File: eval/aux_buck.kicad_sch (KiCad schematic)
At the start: 15 parts, among them U1 AP63205WU-7, U10 TPS7A2033PDBVR, U12 TPS7A2033PDBVR

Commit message: [layout] layout completed, ready for trace
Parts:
- R17: footprint (none) -> Resistor_SMD:R_0603_1608Metric
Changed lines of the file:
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@@
 			)
 		)
-		(property "Footprint" ""
+		(property "Footprint" "Resistor_SMD:R_0603_1608Metric"
 			(at 97.79 118.11 0)
 			(hide yes)

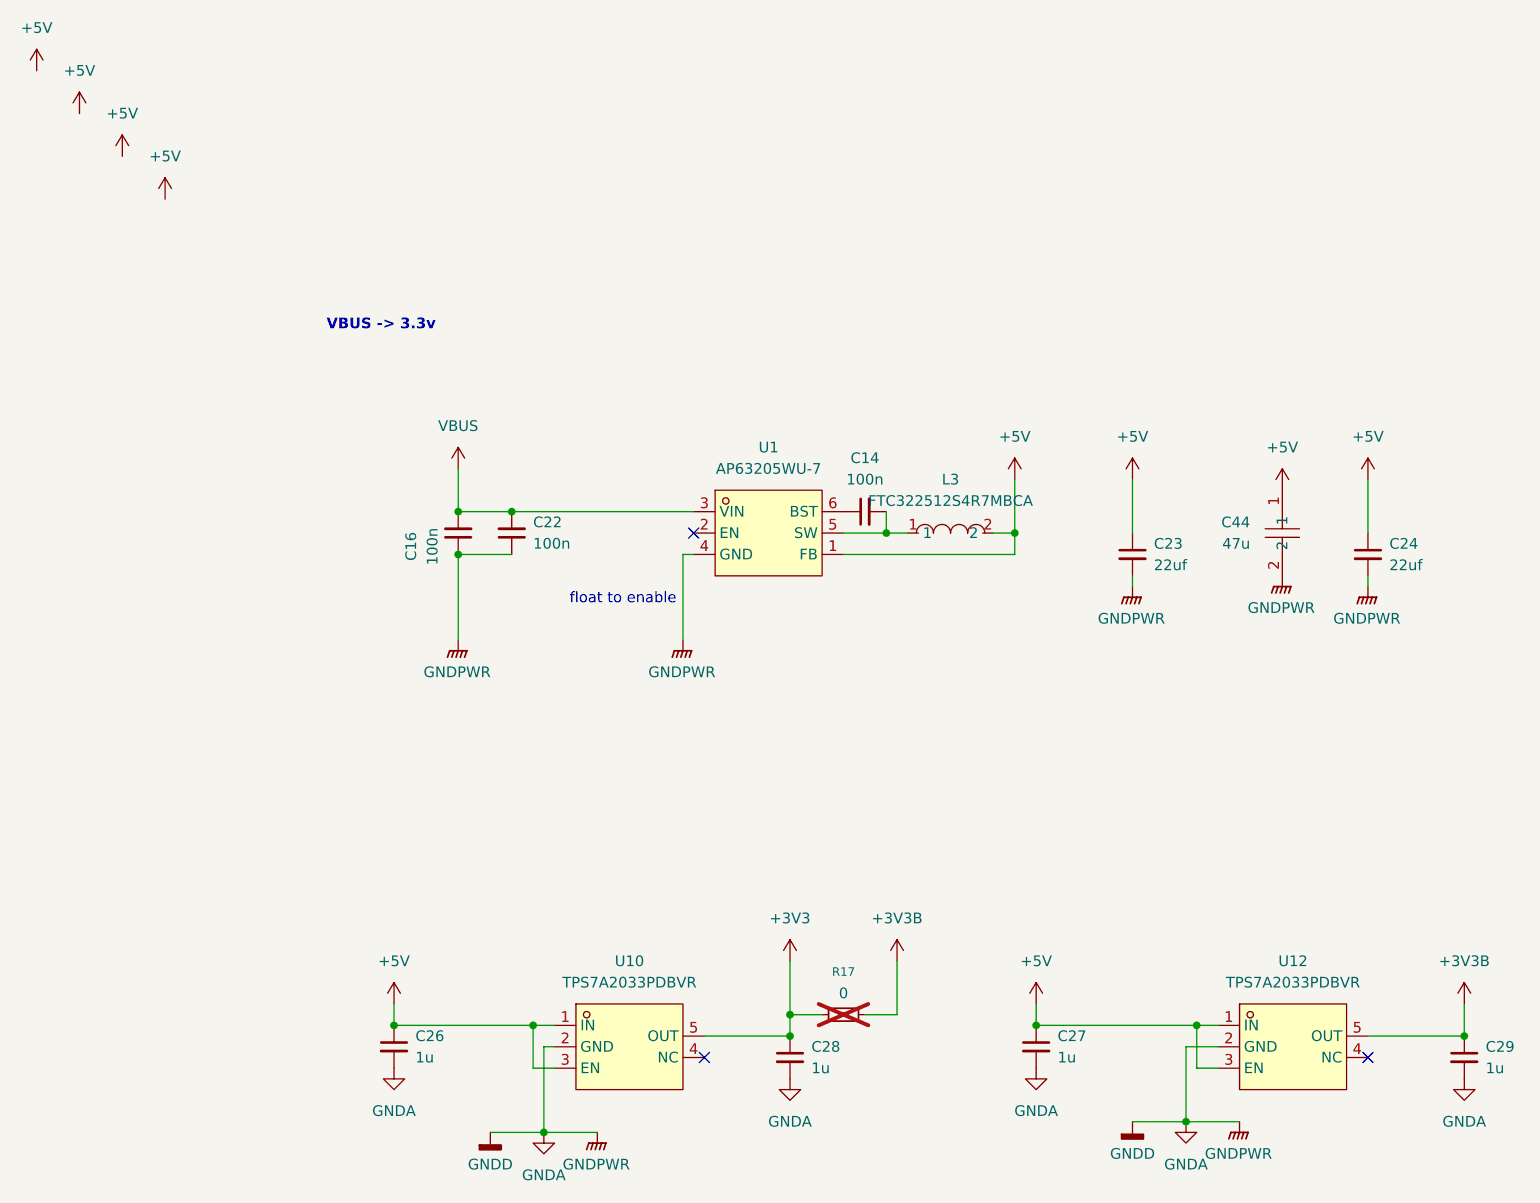
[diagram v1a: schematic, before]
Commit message: [trace] add high power trace
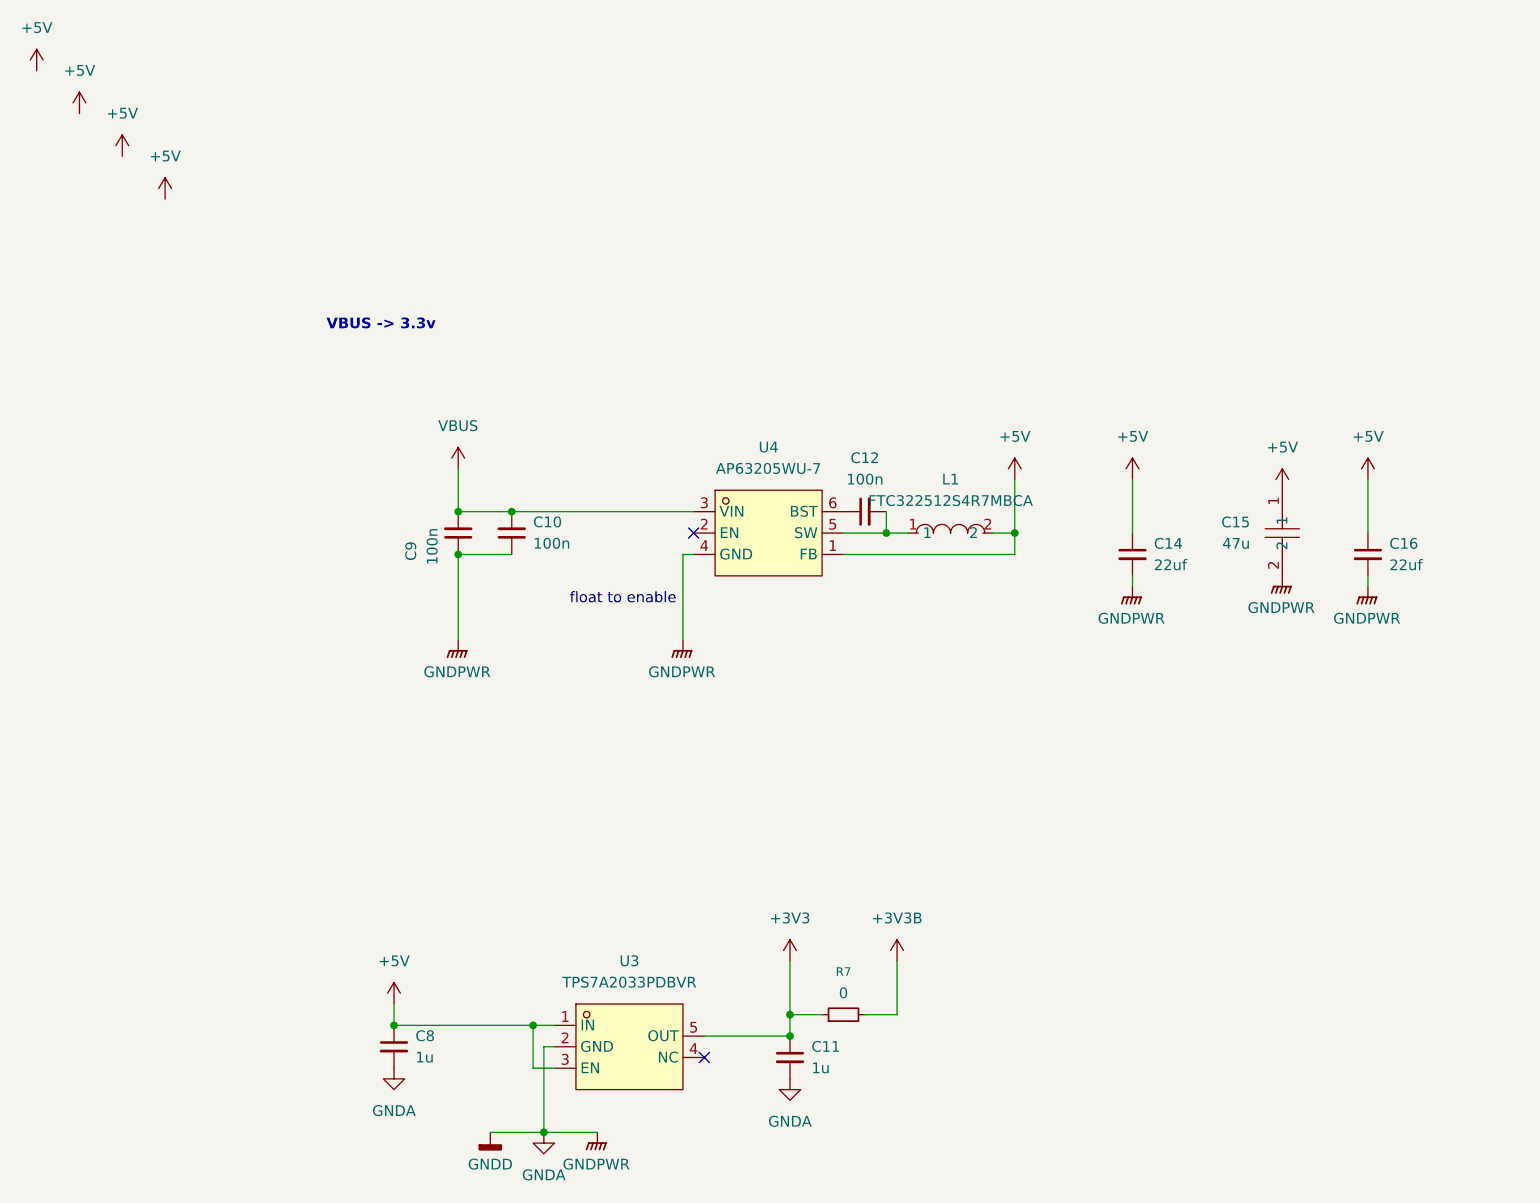
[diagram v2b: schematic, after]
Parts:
- removed C27, C29: 1u, Capacitor_SMD:C_0603_1608Metric, symbol Device:C_Small
- removed U12: TPS7A2033PDBVR, EasyEDA:SOT-23-5_L2.9-W1.6-P0.95-LS2.8-BR, symbol EasyEDA:TPS7A2033PDBVR
- R7: renamed from R17; now fitted
- renumbered C22 to C10, C28 to C11, C14 to C12, C23 to C14, C44 to C15, C24 to C16, C26 to C8, C16 to C9, L3 to L1, U10 to U3, U1 to U4
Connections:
- no-connect marks 3 -> 2
